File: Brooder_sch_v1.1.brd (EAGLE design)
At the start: 80 x 75 mm, 32 parts, among them J1 DCJ0202, J2 1X2-3.5MM, U1 328P

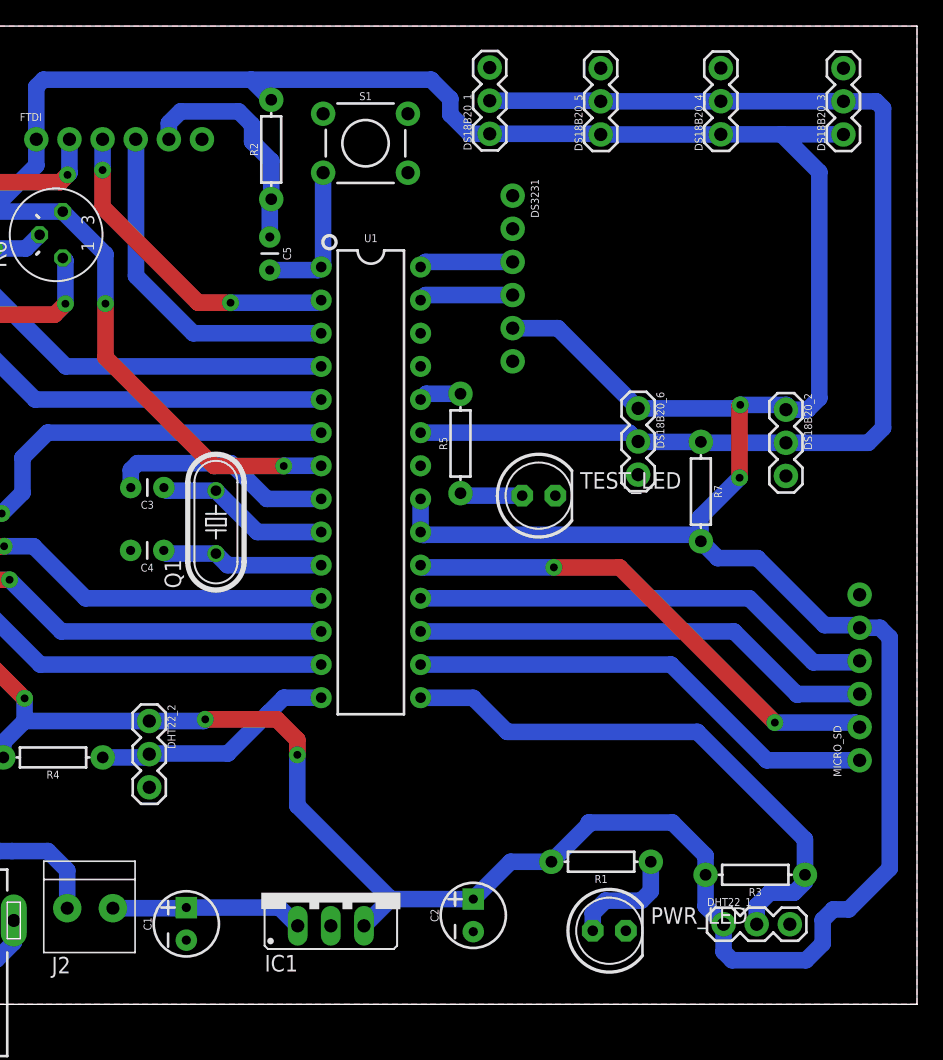
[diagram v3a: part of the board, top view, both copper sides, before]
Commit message: Joins the bottom ground plane into one
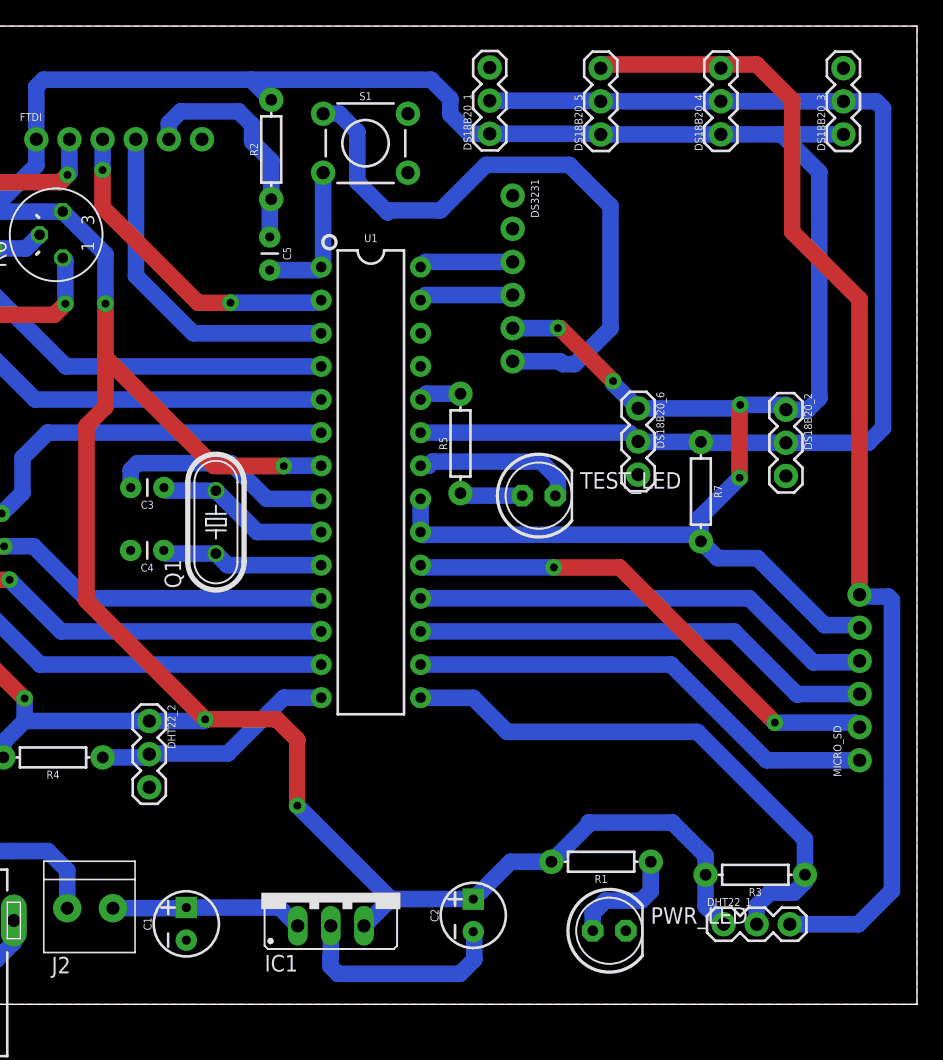
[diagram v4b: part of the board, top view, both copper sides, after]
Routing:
- net GND: track 76.0 -> 243.7 mm
- net 5V: track 347.7 -> 340.5 mm, vias 8 -> 10
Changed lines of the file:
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@@
 <grid distance="0.01" unitdist="mm" unit="mm" style="lines" multiple="1" display="no" altdistance="5" altunitdist="mil" altunit="mil"/>
 <layers>
-<layer number="1" name="Top" color="4" fill="1" visible="yes" active="yes"/>
+<layer number="1" name="Top" color="4" fill="1" visible="no" active="yes"/>
 <layer number="2" name="Route2" color="1" fill="3" visible="no" active="no"/>
 <layer number="3" name="Route3" color="4" fill="3" visible="no" active="no"/>
@@
 <wire x1="9.43" y1="3.43" x2="10.75" y2="4.75" width="1.27" layer="16"/>
 <wire x1="10.75" y1="4.75" x2="10.75" y2="6.43" width="1.27" layer="16"/>
+<wire x1="35.06" y1="6.02" x2="35.06" y2="3.63" width="1.27" layer="16"/>
+<wire x1="35.06" y1="3.63" x2="35.03" y2="3.6" width="1.27" layer="16"/>
+<wire x1="35.03" y1="3.6" x2="35.03" y2="2.91" width="1.27" layer="16"/>
+<wire x1="35.03" y1="2.91" x2="35.6" y2="2.34" width="1.27" layer="16"/>
+<wire x1="35.6" y1="2.34" x2="44.97" y2="2.34" width="1.27" layer="16"/>
+<wire x1="46.06" y1="5.49" x2="45.98" y2="5.57" width="1.27" layer="16"/>
+<wire x1="44.97" y1="2.34" x2="46.06" y2="3.43" width="1.27" layer="16"/>
+<wire x1="46.06" y1="3.43" x2="46.06" y2="5.49" width="1.27" layer="16"/>
+<wire x1="52.47" y1="40.32" x2="52.47" y2="39.2" width="1.27" layer="16"/>
+<wire x1="52.47" y1="39.2" x2="52.27" y2="39" width="1.27" layer="16"/>
+<wire x1="41.94" y1="41.29" x2="42.54" y2="41.29" width="1.27" layer="16"/>
+<wire x1="42.54" y1="41.29" x2="42.86" y2="41.61" width="1.27" layer="16"/>
+<wire x1="42.86" y1="41.61" x2="51.18" y2="41.61" width="1.27" layer="16"/>
+<wire x1="51.18" y1="41.61" x2="52.47" y2="40.32" width="1.27" layer="16"/>
+<wire x1="49" y1="49.3" x2="52.64" y2="49.3" width="1.27" layer="16"/>
+<wire x1="52.64" y1="49.3" x2="52.86" y2="49.08" width="1.27" layer="16"/>
+<wire x1="52.86" y1="49.08" x2="53.76" y2="49.08" width="1.27" layer="16"/>
+<wire x1="56.5" y1="51.82" x2="56.5" y2="61.21" width="1.27" layer="16"/>
+<wire x1="56.5" y1="61.21" x2="53.35" y2="64.36" width="1.27" layer="16"/>
+<wire x1="39.57" y1="60.87" x2="39.43" y2="60.73" width="1.27" layer="16"/>
+<wire x1="39.43" y1="60.73" x2="39.42" y2="60.73" width="1.27" layer="16"/>
+<wire x1="37.09" y1="63.06" x2="37.09" y2="66.9" width="1.27" layer="16"/>
+<wire x1="37.09" y1="66.9" x2="35.7094" y2="68.2806" width="1.27" layer="16"/>
+<wire x1="35.7094" y1="68.2806" x2="34.4688" y2="68.2806" width="1.27" layer="16"/>
+<wire x1="53.76" y1="49.08" x2="56.5" y2="51.82" width="1.27" layer="16"/>
+<wire x1="53.35" y1="64.36" x2="46.96" y2="64.36" width="1.27" layer="16"/>
+<wire x1="46.96" y1="64.36" x2="43.47" y2="60.87" width="1.27" layer="16"/>
+<wire x1="43.47" y1="60.87" x2="39.57" y2="60.87" width="1.27" layer="16"/>
+<wire x1="39.42" y1="60.73" x2="37.09" y2="63.06" width="1.27" layer="16"/>
+<wire x1="75.6" y1="31.41" x2="75.6" y2="54.05" width="1.27" layer="1"/>
+<wire x1="56.04" y1="72.06" x2="55.75" y2="71.77" width="1.27" layer="1"/>
+<wire x1="75.6" y1="54.05" x2="70.43" y2="59.22" width="1.27" layer="1"/>
+<wire x1="70.43" y1="59.22" x2="70.43" y2="69.34" width="1.27" layer="1"/>
+<wire x1="70.43" y1="69.34" x2="67.71" y2="72.06" width="1.27" layer="1"/>
+<wire x1="67.71" y1="72.06" x2="56.04" y2="72.06" width="1.27" layer="1"/>
+<wire x1="70.25" y1="6.14" x2="75.51" y2="6.14" width="1.27" layer="16"/>
+<wire x1="75.51" y1="6.14" x2="78.08" y2="8.71" width="1.27" layer="16"/>
+<wire x1="78.08" y1="8.71" x2="78.08" y2="30.99" width="1.27" layer="16"/>
+<wire x1="78.08" y1="30.99" x2="77.81" y2="31.26" width="1.27" layer="16"/>
+<wire x1="77.81" y1="31.26" x2="75.75" y2="31.26" width="1.27" layer="16"/>
+<wire x1="75.75" y1="31.26" x2="75.6" y2="31.41" width="1.27" layer="16"/>
 </signal>
 <signal name="12V">
@@
 <wire x1="62.93" y1="36" x2="63.43" y2="35.5" width="1.27" layer="16"/>
 <wire x1="42.15" y1="36" x2="62.93" y2="36" width="1.27" layer="16"/>
-<wire x1="58.62" y1="45.69" x2="52.47" y2="51.84" width="1.27" layer="16"/>
 <wire x1="52.47" y1="51.84" x2="49" y2="51.84" width="1.27" layer="16"/>
 <wire x1="47.24" y1="66.74" x2="55.7" y2="66.74" width="1.27" layer="16"/>
@@
 <wire x1="25.3" y1="21.72" x2="25.43" y2="21.85" width="1.27" layer="16"/>
 <via x="25.43" y="21.85" extent="1-16" drill="0.6" diameter="1.3"/>
-<wire x1="30.92" y1="21.85" x2="32.49" y2="20.28" width="1.27" layer="1"/>
-<wire x1="32.49" y1="20.28" x2="32.49" y2="19.13" width="1.27" layer="1"/>
-<via x="32.49" y="19.13" extent="1-16" drill="0.6" diameter="1.3"/>
-<wire x1="32.49" y1="19.13" x2="32.49" y2="15.23" width="1.27" layer="16"/>
+<wire x1="32.49" y1="20.28" x2="30.92" y2="21.85" width="1.27" layer="1"/>
 <wire x1="32.49" y1="15.23" x2="39.65" y2="8.07" width="1.27" layer="16"/>
 <wire x1="28.95" y1="70.89" x2="42.75" y2="70.89" width="1.27" layer="16"/>
@@
 <wire x1="67.77" y1="34.21" x2="64.72" y2="34.21" width="1.27" layer="16"/>
 <wire x1="64.72" y1="34.21" x2="63.43" y2="35.5" width="1.27" layer="16"/>
-<wire x1="75.6" y1="28.87" x2="77.16" y2="28.87" width="1.27" layer="16"/>
-<wire x1="77.16" y1="28.87" x2="77.91" y2="28.12" width="1.27" layer="16"/>
-<wire x1="77.91" y1="28.12" x2="77.91" y2="10.42" width="1.27" layer="16"/>
-<wire x1="74.77" y1="7.28" x2="73.58" y2="7.28" width="1.27" layer="16"/>
-<wire x1="73.58" y1="7.28" x2="72.77" y2="6.47" width="1.27" layer="16"/>
-<wire x1="72.77" y1="6.47" x2="72.77" y2="4.66" width="1.27" layer="16"/>
-<wire x1="72.77" y1="4.66" x2="71.49" y2="3.38" width="1.27" layer="16"/>
-<wire x1="65.17" y1="4.03" x2="65.17" y2="6.14" width="1.27" layer="16"/>
-<wire x1="77.91" y1="10.42" x2="74.77" y2="7.28" width="1.27" layer="16"/>
-<wire x1="71.49" y1="3.38" x2="65.82" y2="3.38" width="1.27" layer="16"/>
-<wire x1="65.82" y1="3.38" x2="65.17" y2="4.03" width="1.27" layer="16"/>
+<via x="32.49" y="15.23" extent="1-16" drill="0.6" diameter="1.3"/>
+<wire x1="32.49" y1="15.23" x2="32.49" y2="20.28" width="1.27" layer="1"/>
+<wire x1="58.62" y1="45.69" x2="56.7" y2="47.61" width="1.27" layer="16"/>
+<wire x1="56.7" y1="47.61" x2="56.7" y2="47.78" width="1.27" layer="16"/>
+<via x="56.7" y="47.78" extent="1-16" drill="0.6" diameter="1.3"/>
+<wire x1="56.7" y1="47.78" x2="52.64" y2="51.84" width="1.27" layer="1"/>
+<wire x1="52.64" y1="51.84" x2="52.47" y2="51.84" width="1.27" layer="1"/>
+<via x="52.47" y="51.84" extent="1-16" drill="0.6" diameter="1.3"/>
+<wire x1="25.43" y1="21.85" x2="16.33" y2="30.95" width="1.27" layer="1"/>
+<wire x1="17.78" y1="45.8" x2="17.78" y2="49.59" width="1.27" layer="1"/>
+<wire x1="16.33" y1="30.95" x2="16.33" y2="44.35" width="1.27" layer="1"/>
+<wire x1="16.33" y1="44.35" x2="17.78" y2="45.8" width="1.27" layer="1"/>
 </signal>
 <signal name="N$3">

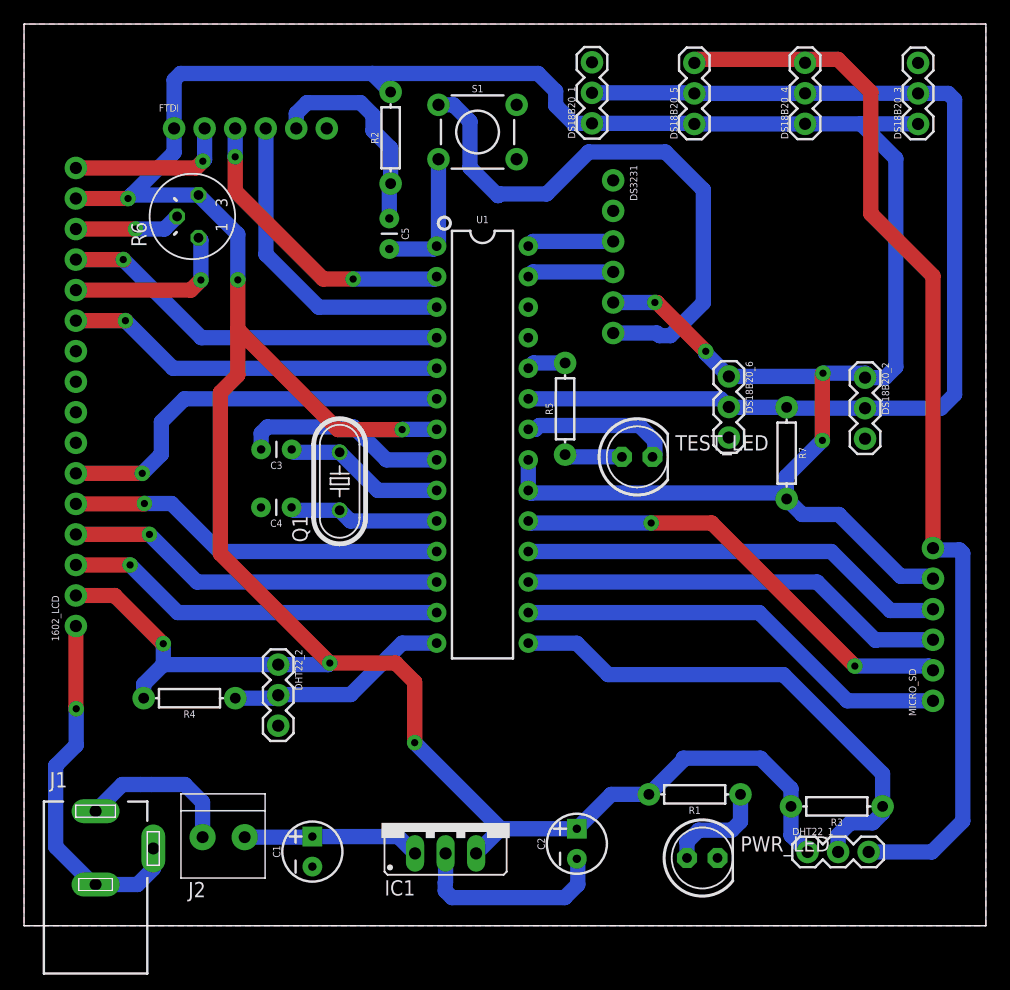
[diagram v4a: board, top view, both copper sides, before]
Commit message: Replaces the 7805 eith the lm2596 buck converter
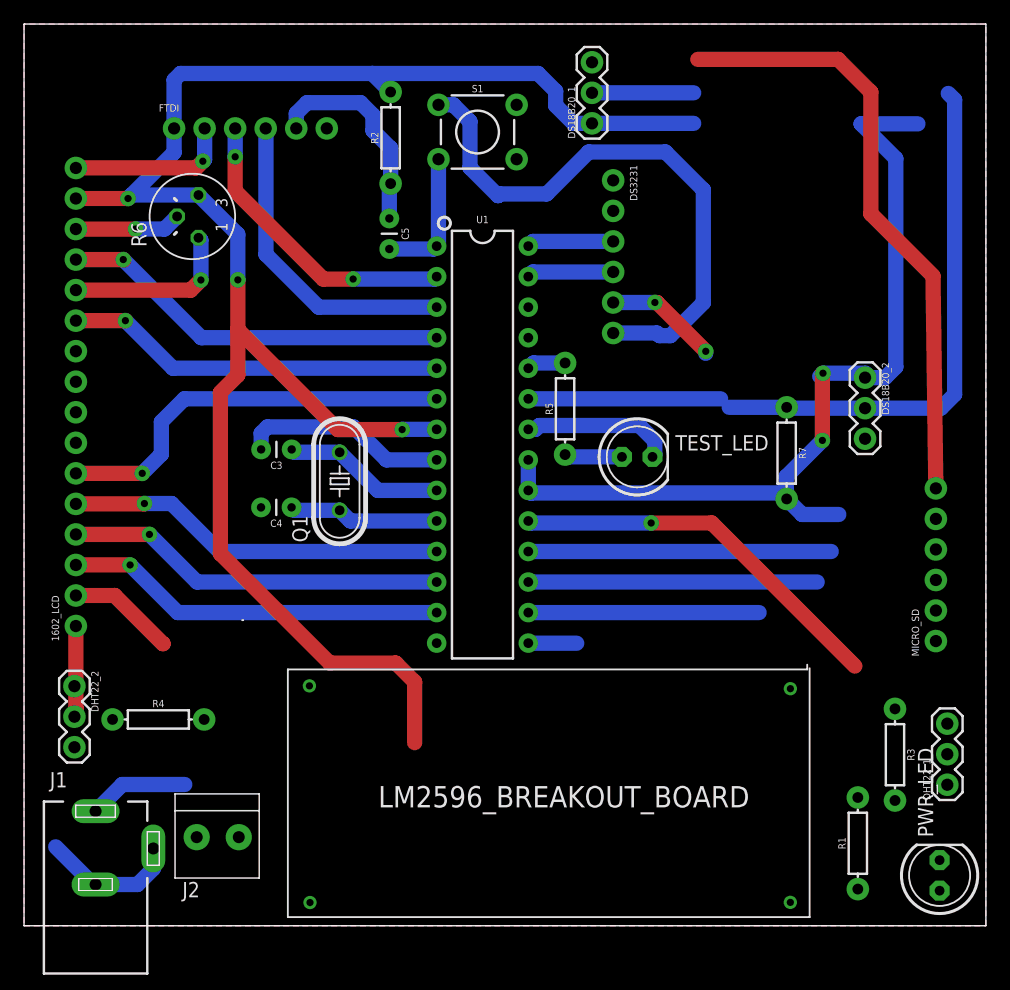
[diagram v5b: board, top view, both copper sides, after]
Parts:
- removed C1, C2: 10uF, SparkFun-Capacitors:CPOL-RADIAL-2.5MM-5MM
- removed DS18B20_3, DS18B20_4, DS18B20_5, DS18B20_6: 455-1750-1-ND, SparkFun-Connectors:1X03
- removed IC1: (no value), v-reg:78XXS
- added U$2: (no value), LM2596_BREAKOUT_BOARD:LM2596_BREAKOUTBOARD
- moved PWR_LED 19.8 mm to (76.2, 4.19), turned to 90 degrees
- moved DHT22_2 17.0 mm to (4.19, 19.9)
- moved R1 14.2 mm to (69.3, 6.86), turned to 90 degrees
- moved DHT22_1 12.9 mm to (76.8, 11.7), turned to 90 degrees
- moved R3 6.47 mm to (72.4, 14.2), turned to 270 degrees
- moved MICRO_SD 4.98 mm to (75.8, 23.7)
- moved R4 3.14 mm to (11.2, 17.2), turned to 0 degrees
- moved J2 0.49 mm to (16.2, 7.37)
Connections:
- net 12V_S: now also U$2.IN(+VE); no longer C1.1, IC1.IN
- net 5V: now also U$2.OUT(+VE); no longer C2.1, DS18B20_3.1, DS18B20_4.1, DS18B20_5.1, DS18B20_6.1, IC1.OUT
- net GND: now also U$2.IN(-VE), U$2.OUT(-VE); no longer C1.2, C2.2, DS18B20_3.3, DS18B20_4.3, DS18B20_5.3, DS18B20_6.3, IC1.GND
- net PC0: no longer DS18B20_3.2, DS18B20_4.2, DS18B20_5.2, DS18B20_6.2
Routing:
- net 5V: track 340.5 -> 240.4 mm, vias 10 -> 7
- net GND: track 243.7 -> 175.3 mm, vias 3 -> 2
- net PB1: track 43.1 -> 4.03 mm
- net PC0: track 91.2 -> 69.0 mm
- net PB0: track 18.6 -> 0.00 mm
- net PB2: track 36.7 -> 19.2 mm
- net 12V_S: track 14.8 -> 0.00 mm
- net PB3: track 35.7 -> 24.0 mm
- net PB4: track 35.7 -> 25.2 mm
- net N$3: track 8.75 -> 0.00 mm
- net PB5: track 38.8 -> 32.2 mm, vias 2 -> 1
- net 12V: track 13.3 -> 8.34 mm

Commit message: Removes four of the six ds18b20 sensor connector
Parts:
- removed R3, R4: 10k, SparkFun-Resistors:AXIAL-0.3
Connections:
- net 5V: no longer R3.P$2, R4.P$2
- net PB0: no longer R4.P$1
- net PB1: no longer R3.P$1
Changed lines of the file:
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@@
 <attribute name="PROD_ID" value="RES-09327" x="30.49" y="65.54" size="1.778" layer="27" rot="R90" display="off"/>
-</element>
-<element name="R3" library="SparkFun-Resistors" package="AXIAL-0.3" value="10k" x="72.44" y="14.23" rot="R270">
-<attribute name="PROD_ID" value="RES-09327" x="72.44" y="14.23" size="1.778" layer="27" rot="R270" display="off"/>
-</element>
-<element name="R4" library="SparkFun-Resistors" package="AXIAL-0.3" value="10k" x="11.17" y="17.16">
-<attribute name="PROD_ID" value="RES-09327" x="11.17" y="17.16" size="1.778" layer="27" display="off"/>
 </element>
 <element name="R7" library="SparkFun-Resistors" package="AXIAL-0.3" value="10k" x="63.43" y="39.31" rot="R270">
@@
 <contactref element="U1" pad="20"/>
 <contactref element="U1" pad="21"/>
-<contactref element="R3" pad="P$2"/>
 <contactref element="DHT22_1" pad="1"/>
-<contactref element="R4" pad="P$2"/>
 <contactref element="DHT22_2" pad="1"/>
 <contactref element="1602_LCD" pad="15"/>
@@
 <wire x1="34.32" y1="41.29" x2="41.94" y2="38.75" width="0" layer="19" extent="1-1"/>
 <wire x1="11.58" y1="23.46" x2="16.33" y2="30.95" width="0" layer="19" extent="1-1"/>
-<wire x1="14.98" y1="17.16" x2="11.58" y2="23.46" width="0" layer="19" extent="1-1"/>
 <wire x1="4.19" y1="19.93" x2="4.31" y2="27.47" width="0" layer="19" extent="1-1"/>
 <wire x1="56.7" y1="47.61" x2="66.18" y2="45.69" width="0" layer="19" extent="16-16"/>
 <wire x1="63.74" y1="19.72" x2="64.72" y2="34.21" width="0" layer="19" extent="16-16"/>
 <wire x1="69.35" y1="10.67" x2="63.74" y2="19.72" width="0" layer="19" extent="1-1"/>
-<wire x1="72.44" y1="10.42" x2="69.35" y2="10.67" width="0" layer="19" extent="1-1"/>
-<wire x1="76.79" y1="11.73" x2="72.44" y2="10.42" width="0" layer="19" extent="1-1"/>
+<wire x1="76.79" y1="11.73" x2="69.35" y2="10.67" width="0" layer="19" extent="1-1"/>
 </signal>
 <signal name="N$3">
@@
 <contactref element="U1" pad="14"/>
 <contactref element="DHT22_2" pad="2"/>
-<contactref element="R4" pad="P$1"/>
-<wire x1="7.36" y1="17.16" x2="34.32" y2="23.51" width="0" layer="19" extent="1-1"/>
-<wire x1="4.19" y1="17.39" x2="7.36" y2="17.16" width="0" layer="19" extent="1-1"/>
+<wire x1="4.19" y1="17.39" x2="34.32" y2="23.51" width="0" layer="19" extent="1-1"/>
 </signal>
 <signal name="PB1">
 <contactref element="U1" pad="15"/>
 <contactref element="DHT22_1" pad="2"/>
-<contactref element="R3" pad="P$1"/>
 <wire x1="45.97" y1="23.5" x2="41.95" y2="23.5" width="1.27" layer="16"/>
 <wire x1="41.95" y1="23.5" x2="41.94" y2="23.51" width="1.27" layer="16"/>
-<wire x1="72.44" y1="18.04" x2="76.79" y2="14.27" width="0" layer="19" extent="1-1"/>
-<wire x1="45.97" y1="23.5" x2="72.44" y2="18.04" width="0" layer="19" extent="16-16"/>
+<wire x1="45.97" y1="23.5" x2="76.79" y2="14.27" width="0" layer="19" extent="16-16"/>
 </signal>
 <signal name="PB4">
